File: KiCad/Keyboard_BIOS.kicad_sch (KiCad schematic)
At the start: 18 parts, among them J1 Keyboard, J2 Mouse, J22 Keylock: Unlocked/Locked, U1 8242KBD, U14 SST39SF010A, U61 74LS06

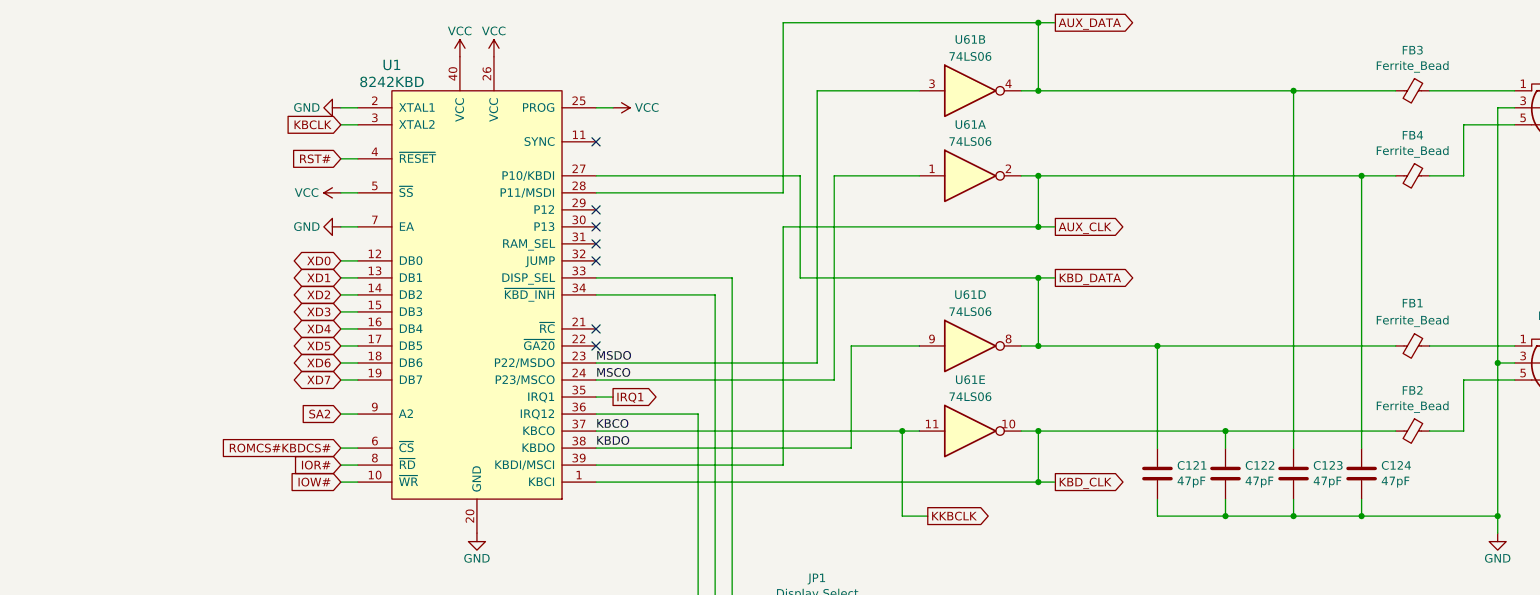
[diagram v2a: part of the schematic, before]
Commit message: More schematic updates. Remove old KiCad files
Signed-off-by: Sergey Kiselev <skiselev@gmail.com>
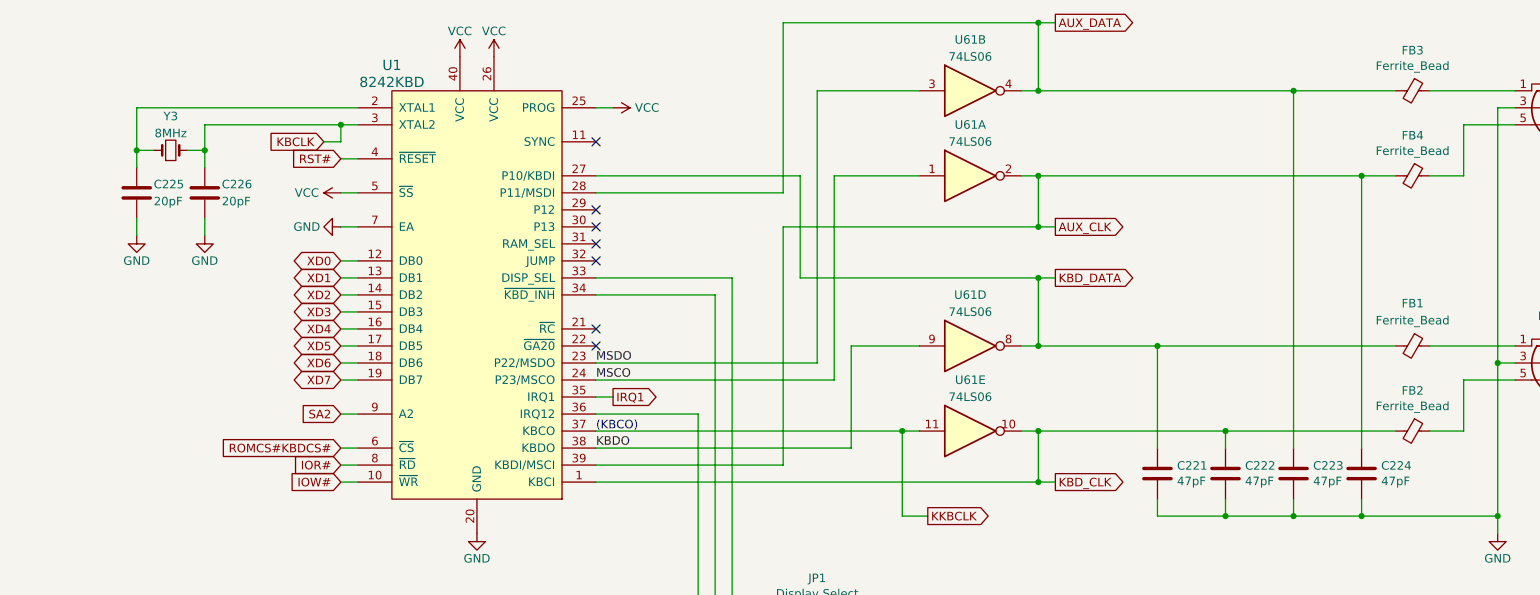
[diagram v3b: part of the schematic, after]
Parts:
- added C225, C226: 20pF, Capacitor_SMD:C_0603_1608Metric_Pad1.08x0.95mm_HandSolder, symbol Device:C
- added Y3: 8MHz, My_Components:Crystal_32K_Horiz, symbol Device:Crystal_Small
- renumbered C121 to C221, C122 to C222, C123 to C223, C124 to C224
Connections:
- net GND: now also C225.2, C226.2; no longer U1.2 (XTAL1)
- net KBCLK: now also C226.1, Y3.2
- new net: C225.1, U1.2 (XTAL1), Y3.1
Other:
- note added: "(KBCO)"
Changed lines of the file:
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@@
   (junction (at 236.22 99.06) (diameter 0) (color 0 0 0 0)
   )
+  (junction (at 63.5 40.64) (diameter 0) (color 0 0 0 0)
+  )
   (junction (at 167.64 48.26) (diameter 0) (color 0 0 0 0)
   )
@@
   (junction (at 167.64 73.66) (diameter 0) (color 0 0 0 0)
   )
+  (junction (at 43.18 44.45) (diameter 0) (color 0 0 0 0)
+  )
   (junction (at 167.64 86.36) (diameter 0) (color 0 0 0 0)
   )
@@
   )
   (junction (at 236.22 76.2) (diameter 0) (color 0 0 0 0)
+  )
+  (junction (at 33.02 44.45) (diameter 0) (color 0 0 0 0)
   )
   (junction (at 215.9 99.06) (diameter 0) (color 0 0 0 0)
@@
     (stroke (width 0) (type default) (color 0 0 0 0))
   )
+  (wire (pts (xy 33.02 44.45) (xy 35.56 44.45))
+    (stroke (width 0) (type default) (color 0 0 0 0))
+  )
   (wire (pts (xy 101.6 129.54) (xy 99.06 129.54))
     (stroke (width 0) (type default) (color 0 0 0 0))
@@
     (stroke (width 0) (type default) (color 0 0 0 0))
   )
+  (wire (pts (xy 43.18 57.15) (xy 43.18 54.61))
+    (stroke (width 0) (type default) (color 0 0 0 0))
+  )
   (wire (pts (xy 139.7 88.9) (xy 101.6 88.9))
     (stroke (width 0) (type default) (color 0 0 0 0))
@@
     (stroke (width 0) (type default) (color 0 0 0 0))
   )
+  (wire (pts (xy 33.02 38.1) (xy 33.02 44.45))
+    (stroke (width 0) (type default) (color 0 0 0 0))
+  )
   (wire (pts (xy 205.74 99.06) (xy 215.9 99.06))
     (stroke (width 0) (type default) (color 0 0 0 0))
@@
     (stroke (width 0) (type default) (color 0 0 0 0))
   )
+  (wire (pts (xy 33.02 57.15) (xy 33.02 54.61))
+    (stroke (width 0) (type default) (color 0 0 0 0))
+  )
   (wire (pts (xy 236.22 76.2) (xy 236.22 99.06))
     (stroke (width 0) (type default) (color 0 0 0 0))
@@
     (stroke (width 0) (type default) (color 0 0 0 0))
   )
+  (wire (pts (xy 63.5 43.18) (xy 63.5 40.64))
+    (stroke (width 0) (type default) (color 0 0 0 0))
+  )
   (wire (pts (xy 238.76 38.1) (xy 236.22 38.1))
     (stroke (width 0) (type default) (color 0 0 0 0))
@@
     (stroke (width 0) (type default) (color 0 0 0 0))
   )
+  (wire (pts (xy 43.18 46.99) (xy 43.18 44.45))
+    (stroke (width 0) (type default) (color 0 0 0 0))
+  )
   (wire (pts (xy 129.54 91.44) (xy 129.54 55.88))
     (stroke (width 0) (type default) (color 0 0 0 0))
@@
     (stroke (width 0) (type default) (color 0 0 0 0))
   )
+  (wire (pts (xy 43.18 44.45) (xy 43.18 40.64))
+    (stroke (width 0) (type default) (color 0 0 0 0))
+  )
   (wire (pts (xy 121.92 114.3) (xy 121.92 63.5))
     (stroke (width 0) (type default) (color 0 0 0 0))
@@
     (stroke (width 0) (type default) (color 0 0 0 0))
   )
+  (wire (pts (xy 33.02 44.45) (xy 33.02 46.99))
+    (stroke (width 0) (type default) (color 0 0 0 0))
+  )
   (wire (pts (xy 101.6 91.44) (xy 129.54 91.44))
     (stroke (width 0) (type default) (color 0 0 0 0))
   )
+  (wire (pts (xy 60.96 43.18) (xy 63.5 43.18))
+    (stroke (width 0) (type default) (color 0 0 0 0))
+  )
   (wire (pts (xy 167.64 55.88) (xy 167.64 48.26))
     (stroke (width 0) (type default) (color 0 0 0 0))
@@
     (stroke (width 0) (type default) (color 0 0 0 0))
   )
+  (wire (pts (xy 43.18 44.45) (xy 40.64 44.45))
+    (stroke (width 0) (type default) (color 0 0 0 0))
+  )
   (wire (pts (xy 101.6 137.16) (xy 99.06 137.16))
     (stroke (width 0) (type default) (color 0 0 0 0))
   )
-  (wire (pts (xy 63.5 38.1) (xy 66.04 38.1))
+  (wire (pts (xy 33.02 38.1) (xy 66.04 38.1))
+    (stroke (width 0) (type default) (color 0 0 0 0))
+  )
+  (wire (pts (xy 63.5 40.64) (xy 43.18 40.64))
     (stroke (width 0) (type default) (color 0 0 0 0))
   )
@@
   (wire (pts (xy 101.6 76.2) (xy 134.62 76.2))
     (stroke (width 0) (type default) (color 0 0 0 0))
+  )
+  (text "(KBCO)" (at 101.6 86.36 0)
+    (effects (font (size 1.27 1.27)) (justify left bottom))
   )
   (label "KBDO" (at 101.6 88.9 0)
     (effects (font (size 1.27 1.27)) (justify left bottom))
   )
-  (label "KBCO" (at 101.6 86.36 0)
-    (effects (font (size 1.27 1.27)) (justify left bottom))
-  )
   (label "IRQ12_AUX" (at 129.54 142.24 180)
     (effects (font (size 1.27 1.27)) (justify right bottom))
@@
     (effects (font (size 1.27 1.27)) (justify right))
     (property "Intersheet References" "${INTERSHEET_REFS}" (id 0) (at 56.7006 91.3606 0)
+      (effects (font (size 1.27 1.27)) (justify right) hide)
+    )
+  )
+  (global_label "KBCLK" (shape input) (at 60.96 43.18 180) (fields_autoplaced)
+    (effects (font (size 1.27 1.27)) (justify right))
+    (property "Intersheet References" "${INTERSHEET_REFS}" (id 0) (at 52.5277 43.1006 0)
       (effects (font (size 1.27 1.27)) (justify right) hide)
     )
@@
     (property "Intersheet References" "${INTERSHEET_REFS}" (id 0) (at 0 0 0)
       (effects (font (size 1.27 1.27)) hide)
-    )
-  )
-  (global_label "KBCLK" (shape input) (at 63.5 40.64 180) (fields_autoplaced)
-    (effects (font (size 1.27 1.27)) (justify right))
-    (property "Intersheet References" "${INTERSHEET_REFS}" (id 0) (at 55.0677 40.5606 0)
-      (effects (font (size 1.27 1.27)) (justify right) hide)
     )
   )
@@
     (pin "1")
   )
-  (symbol (lib_id "power:GND") (at 63.5 38.1 270) (unit 1)
-    (in_bom yes) (on_board yes)
-    (property "Reference" "#PWR0263" (id 0) (at 57.15 38.1 0)
-      (effects (font (size 1.27 1.27)) hide)
-    )
-    (property "Value" "GND" (id 1) (at 58.42 38.1 90))
-    (property "Footprint" "" (id 2) (at 63.5 38.1 0)
-      (effects (font (size 1.27 1.27)) hide)
-    )
-    (property "Datasheet" "" (id 3) (at 63.5 38.1 0)
-      (effects (font (size 1.27 1.27)) hide)
-    )
-    (pin "1")
-  )
   (symbol (lib_id "power:VCC") (at 63.5 50.8 90) (unit 1)
     (in_bom yes) (on_board yes)
@@
   (symbol (lib_id "Device:C") (at 185.42 92.71 0) (unit 1)
     (in_bom yes) (on_board yes)
-    (property "Reference" "C121" (id 0) (at 188.341 91.5416 0)
+    (property "Reference" "C221" (id 0) (at 188.341 91.5416 0)
       (effects (font (size 1.27 1.27)) (justify left))
     )
@@
   (symbol (lib_id "Device:C") (at 195.58 92.71 0) (unit 1)
     (in_bom yes) (on_board yes)
-    (property "Reference" "C122" (id 0) (at 198.501 91.5416 0)
+    (property "Reference" "C222" (id 0) (at 198.501 91.5416 0)
       (effects (font (size 1.27 1.27)) (justify left))
     )
@@
   (symbol (lib_id "Device:C") (at 205.74 92.71 0) (unit 1)
     (in_bom yes) (on_board yes)
-    (property "Reference" "C123" (id 0) (at 208.661 91.5416 0)
+    (property "Reference" "C223" (id 0) (at 208.661 91.5416 0)
       (effects (font (size 1.27 1.27)) (justify left))
     )
@@
   (symbol (lib_id "Device:C") (at 215.9 92.71 0) (unit 1)
     (in_bom yes) (on_board yes)
-    (property "Reference" "C124" (id 0) (at 218.821 91.5416 0)
+    (property "Reference" "C224" (id 0) (at 218.821 91.5416 0)
       (effects (font (size 1.27 1.27)) (justify left))
     )
@@
       (effects (font (size 1.27 1.27)) hide)
     )
+    (pin "1")
+  )
+  (symbol (lib_id "Device:Crystal_Small") (at 38.1 44.45 0) (unit 1)
+    (in_bom yes) (on_board yes)
+    (property "Reference" "Y3" (id 0) (at 38.1 39.37 0))
+    (property "Value" "8MHz" (id 1) (at 38.1 41.91 0))
+    (property "Footprint" "My_Components:Crystal_32K_Horiz" (id 2) (at 38.1 44.45 0)
+      (effects (font (size 1.27 1.27)) hide)
+    )
+    (property "Datasheet" "~" (id 3) (at 38.1 44.45 0)
+      (effects (font (size 1.27 1.27)) hide)
+    )
+    (pin "1")
+    (pin "2")
+  )
+  (symbol (lib_id "Device:C") (at 33.02 50.8 0) (unit 1)
+    (in_bom yes) (on_board yes)
+    (property "Reference" "C225" (id 0) (at 35.56 49.53 0)
+      (effects (font (size 1.27 1.27)) (justify left))
+    )
+    (property "Value" "20pF" (id 1) (at 35.56 52.07 0)
+      (effects (font (size 1.27 1.27)) (justify left))
+    )
+    (property "Footprint" "Capacitor_SMD:C_0603_1608Metric_Pad1.08x0.95mm_HandSolder" (id 2) (at 33.9852 54.61 0)
+      (effects (font (size 1.27 1.27)) hide)
+    )
+    (property "Datasheet" "~" (id 3) (at 33.02 50.8 0)
+      (effects (font (size 1.27 1.27)) hide)
+    )
+    (pin "1")
+    (pin "2")
+  )
+  (symbol (lib_id "power:GND") (at 43.18 57.15 0) (unit 1)
+    (in_bom yes) (on_board yes)
+    (property "Reference" "#PWR0492" (id 0) (at 43.18 63.5 0)
+      (effects (font (size 1.27 1.27)) hide)
+    )
+    (property "Value" "GND" (id 1) (at 43.18 60.96 0))
+    (property "Footprint" "" (id 2) (at 43.18 57.15 0)
+      (effects (font (size 1.27 1.27)) hide)
+    )
+    (property "Datasheet" "" (id 3) (at 43.18 57.15 0)
+      (effects (font (size 1.27 1.27)) hide)
+    )
+    (pin "1")
+  )
+  (symbol (lib_id "Device:C") (at 43.18 50.8 0) (unit 1)
+    (in_bom yes) (on_board yes)
+    (property "Reference" "C226" (id 0) (at 45.72 49.53 0)
+      (effects (font (size 1.27 1.27)) (justify left))
+    )
+    (property "Value" "20pF" (id 1) (at 45.72 52.07 0)
+      (effects (font (size 1.27 1.27)) (justify left))
+    )
+    (property "Footprint" "Capacitor_SMD:C_0603_1608Metric_Pad1.08x0.95mm_HandSolder" (id 2) (at 44.1452 54.61 0)
+      (effects (font (size 1.27 1.27)) hide)
+    )
+    (property "Datasheet" "~" (id 3) (at 43.18 50.8 0)
+      (effects (font (size 1.27 1.27)) hide)
+    )
+    (pin "1")
+    (pin "2")
+  )
+  (symbol (lib_id "power:GND") (at 33.02 57.15 0) (unit 1)
+    (in_bom yes) (on_board yes)
+    (property "Reference" "#PWR0491" (id 0) (at 33.02 63.5 0)
+      (effects (font (size 1.27 1.27)) hide)
+    )
+    (property "Value" "GND" (id 1) (at 33.02 60.96 0))
+    (property "Footprint" "" (id 2) (at 33.02 57.15 0)
+      (effects (font (size 1.27 1.27)) hide)
+    )
+    (property "Datasheet" "" (id 3) (at 33.02 57.15 0)
+      (effects (font (size 1.27 1.27)) hide)
+    )
